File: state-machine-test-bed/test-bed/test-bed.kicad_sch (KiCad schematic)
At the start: 19 parts, among them U1 NodeMCU

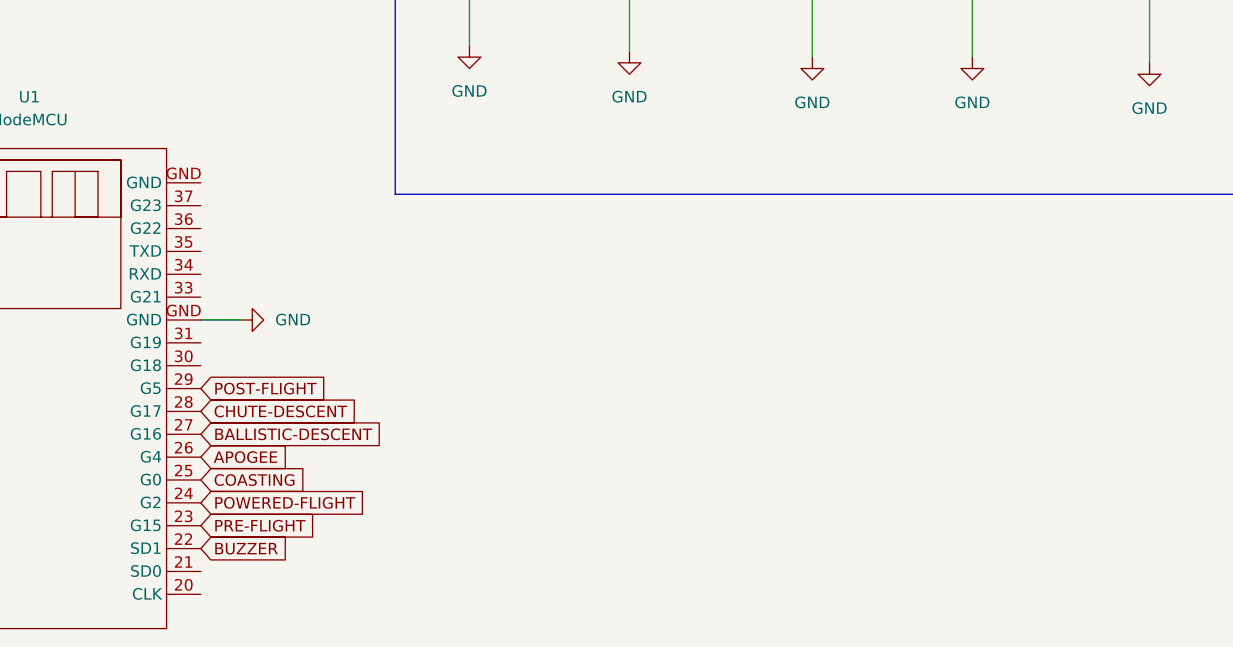
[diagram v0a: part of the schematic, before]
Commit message: finished routing for state-machine test board
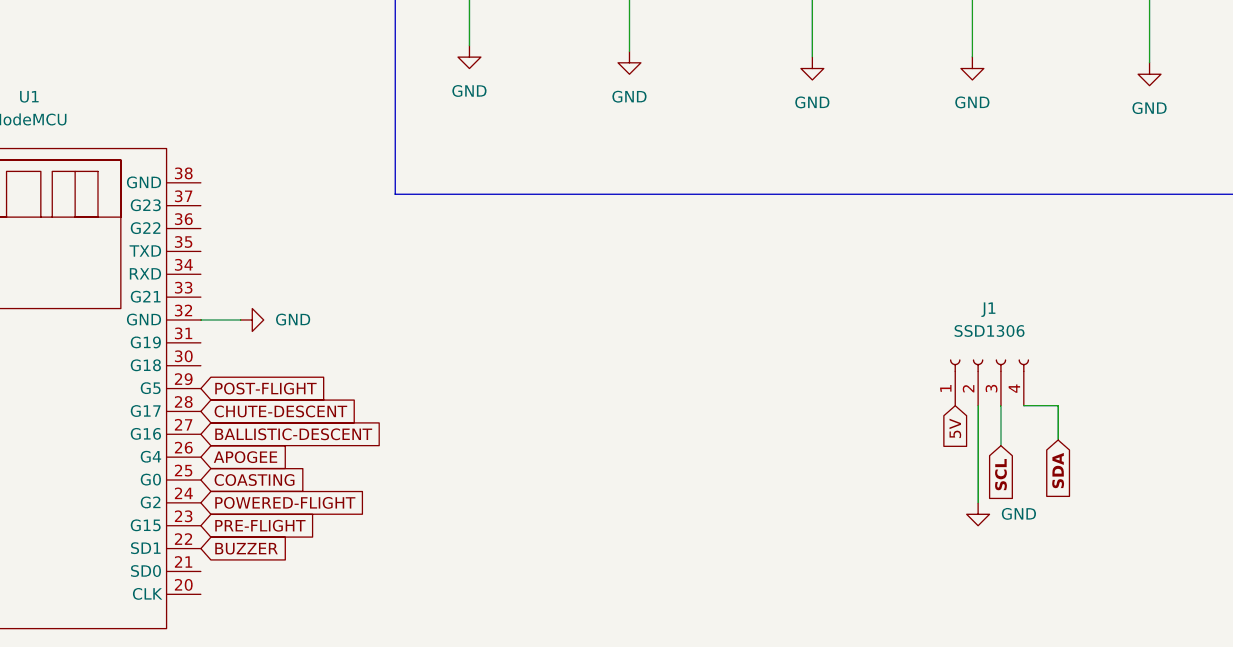
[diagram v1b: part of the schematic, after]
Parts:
- added J1: SSD1306, Connector_PinHeader_2.54mm:PinHeader_1x04_P2.54mm_Vertical, symbol Connector:Conn_01x04_Female
- U1: footprint (none) -> custom-footprints:NODEMCU
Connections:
- net 5V: now also J1.1 (Pin_1)
- net GND: now also U1.32 (GND), J1.2 (Pin_2); no longer U1.GND
- new net SCL: J1.3 (Pin_3)
- new net SDA: J1.4 (Pin_4)
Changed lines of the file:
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@@
+    (stroke (width 0) (type default) (color 0 0 0 0))
+  )
+  (wire (pts (xy 178.435 140.335) (xy 178.435 135.89))
     (stroke (width 0) (type default) (color 0 0 0 0))
   )
@@
     (stroke (width 0) (type default) (color 0 0 0 0))
   )
+  (wire (pts (xy 175.895 135.89) (xy 175.895 146.685))
+    (stroke (width 0) (type default) (color 0 0 0 0))
+  )
   (wire (pts (xy 62.23 65.405) (xy 62.23 67.945))
     (stroke (width 0) (type default) (color 0 0 0 0))
@@
     (stroke (width 0) (type default) (color 0 0 0 0))
   )
+  (wire (pts (xy 184.785 139.7) (xy 184.785 135.89))
+    (stroke (width 0) (type default) (color 0 0 0 0))
+  )
   (wire (pts (xy 137.16 86.36) (xy 137.16 96.52))
     (stroke (width 0) (type default) (color 0 0 0 0))
@@
   )
   (wire (pts (xy 194.945 75.565) (xy 194.945 80.01))
+    (stroke (width 0) (type default) (color 0 0 0 0))
+  )
+  (wire (pts (xy 184.785 135.89) (xy 180.975 135.89))
     (stroke (width 0) (type default) (color 0 0 0 0))
   )
@@
     (property "Intersheet References" "${INTERSHEET_REFS}" (id 0) (at 99.2052 141.5256 0)
       (effects (font (size 1.27 1.27)) (justify left) hide)
+    )
+  )
+  (global_label "SCL" (shape input) (at 178.435 140.335 270) (fields_autoplaced)
+    (effects (font (size 1.27 1.27) bold) (justify right))
+    (property "Intersheet References" "${INTERSHEET_REFS}" (id 0) (at 178.308 146.4461 90)
+      (effects (font (size 1.27 1.27) bold) (justify right) hide)
+    )
+  )
+  (global_label "5V" (shape input) (at 173.355 135.89 270) (fields_autoplaced)
+    (effects (font (size 1.27 1.27)) (justify right))
+    (property "Intersheet References" "${INTERSHEET_REFS}" (id 0) (at 173.4344 140.6012 90)
+      (effects (font (size 1.27 1.27)) (justify right) hide)
     )
   )
@@
     )
   )
+  (global_label "SDA" (shape input) (at 184.785 139.7 270) (fields_autoplaced)
+    (effects (font (size 1.27 1.27) bold) (justify right))
+    (property "Intersheet References" "${INTERSHEET_REFS}" (id 0) (at 184.658 145.8716 90)
+      (effects (font (size 1.27 1.27) bold) (justify right) hide)
+    )
+  )
   (global_label "BALLISTIC-DESCENT" (shape input) (at 89.535 139.065 0) (fields_autoplaced)
     (effects (font (size 1.27 1.27)) (justify left))
@@
     (pin "2")
   )
+  (symbol (lib_id "power:GND") (at 175.895 146.685 0) (unit 1)
+    (in_bom yes) (on_board yes) (fields_autoplaced)
+    (property "Reference" "#PWR0101" (id 0) (at 175.895 153.035 0)
+      (effects (font (size 1.27 1.27)) hide)
+    )
+    (property "Value" "GND" (id 1) (at 178.435 147.9549 0)
+      (effects (font (size 1.27 1.27)) (justify left))
+    )
+    (property "Footprint" "" (id 2) (at 175.895 146.685 0)
+      (effects (font (size 1.27 1.27)) hide)
+    )
+    (property "Datasheet" "" (id 3) (at 175.895 146.685 0)
+      (effects (font (size 1.27 1.27)) hide)
+    )
+    (pin "1")
+  )
   (symbol (lib_id "Device:LED") (at 157.48 83.185 90) (unit 1)
     (in_bom yes) (on_board yes) (fields_autoplaced)
@@
     (pin "1")
   )
+  (symbol (lib_id "Connector:Conn_01x04_Female") (at 175.895 130.81 90) (unit 1)
+    (in_bom yes) (on_board yes) (fields_autoplaced)
+    (property "Reference" "J1" (id 0) (at 177.165 125.095 90))
+    (property "Value" "SSD1306" (id 1) (at 177.165 127.635 90))
+    (property "Footprint" "Connector_PinHeader_2.54mm:PinHeader_1x04_P2.54mm_Vertical" (id 2) (at 175.895 130.81 0)
+      (effects (font (size 1.27 1.27)) hide)
+    )
+    (property "Datasheet" "~" (id 3) (at 175.895 130.81 0)
+      (effects (font (size 1.27 1.27)) hide)
+    )
+    (pin "1")
+    (pin "2")
+    (pin "3")
+    (pin "4")
+  )
   (symbol (lib_id "power:GND") (at 119.38 95.885 0) (unit 1)
     (in_bom yes) (on_board yes) (fields_autoplaced)
@@
     (property "Reference" "U1" (id 0) (at 70.485 101.6 0))
     (property "Value" "NodeMCU" (id 1) (at 70.485 104.14 0))
-    (property "Footprint" "" (id 2) (at 55.245 107.315 0)
+    (property "Footprint" "custom-footprints:NODEMCU" (id 2) (at 55.245 107.315 0)
       (effects (font (size 1.27 1.27)) hide)
     )
@@
     (pin "30")
     (pin "31")
+    (pin "32")
     (pin "33")
     (pin "34")
@@
     (pin "36")
     (pin "37")
+    (pin "38")
     (pin "4")
     (pin "5")
@@
     (pin "8")
     (pin "9")
-    (pin "GND")
-    (pin "GND")
   )
   (symbol (lib_id "Device:R_Small") (at 62.23 62.865 0) (unit 1)
@@
       (reference "#PWR010") (unit 1) (value "GND") (footprint "")
     )
+    (path "/0b380a55-36ff-4778-9cdc-b02441948baa"
+      (reference "#PWR0101") (unit 1) (value "GND") (footprint "")
+    )
     (path "/d032fdb7-8939-4b34-8544-51d402110347"
       (reference "BT1") (unit 1) (value "7.4 V") (footprint "TerminalBlock:TerminalBlock_Altech_AK300-2_P5.00mm")
@@
       (reference "D7") (unit 1) (value "LED") (footprint "LED_THT:LED_D3.0mm")
     )
+    (path "/82159891-b8dc-4a83-81a3-4855ac694eb8"
+      (reference "J1") (unit 1) (value "SSD1306") (footprint "Connector_PinHeader_2.54mm:PinHeader_1x04_P2.54mm_Vertical")
+    )
     (path "/9615cde7-e48b-4f74-a980-fd982304735c"
       (reference "R1") (unit 1) (value "1k") (footprint "Resistor_THT:R_Axial_DIN0207_L6.3mm_D2.5mm_P10.16mm_Horizontal")
@@
     )
     (path "/912ce666-b718-4561-bae4-91b3c3098c58"
-      (reference "U1") (unit 1) (value "NodeMCU") (footprint "")
-    )
-  )
+      (reference "U1") (unit 1) (value "NodeMCU") (footprint "custom-footprints:NODEMCU")
+    )
+  )

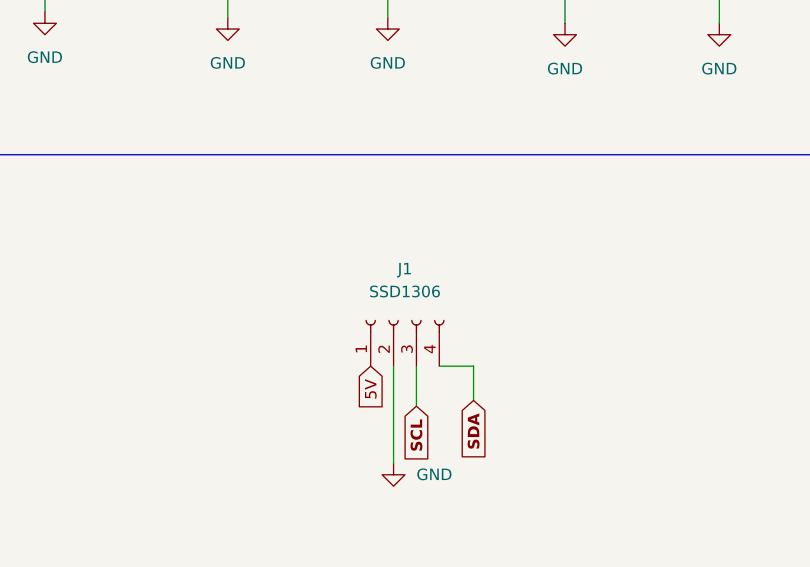
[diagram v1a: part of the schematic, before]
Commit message: finished routing for state-machine test board
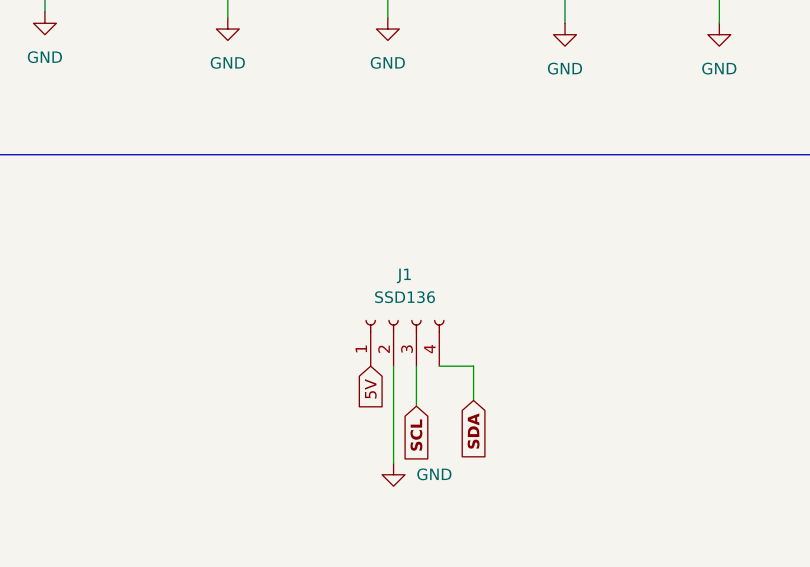
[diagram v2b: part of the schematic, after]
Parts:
- J1: value SSD1306 -> SSD136
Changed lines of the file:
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@@
   (symbol (lib_id "Connector:Conn_01x04_Female") (at 175.895 130.81 90) (unit 1)
     (in_bom yes) (on_board yes) (fields_autoplaced)
-    (property "Reference" "J1" (id 0) (at 177.165 125.095 90))
-    (property "Value" "SSD1306" (id 1) (at 177.165 127.635 90))
+    (property "Reference" "J1" (id 0) (at 177.165 125.73 90))
+    (property "Value" "SSD136" (id 1) (at 177.165 128.27 90))
     (property "Footprint" "Connector_PinHeader_2.54mm:PinHeader_1x04_P2.54mm_Vertical" (id 2) (at 175.895 130.81 0)
       (effects (font (size 1.27 1.27)) hide)
@@
     )
     (path "/82159891-b8dc-4a83-81a3-4855ac694eb8"
-      (reference "J1") (unit 1) (value "SSD1306") (footprint "Connector_PinHeader_2.54mm:PinHeader_1x04_P2.54mm_Vertical")
+      (reference "J1") (unit 1) (value "SSD136") (footprint "Connector_PinHeader_2.54mm:PinHeader_1x04_P2.54mm_Vertical")
     )
     (path "/9615cde7-e48b-4f74-a980-fd982304735c"
